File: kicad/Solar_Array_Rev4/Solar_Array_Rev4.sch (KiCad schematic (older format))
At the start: 23 parts

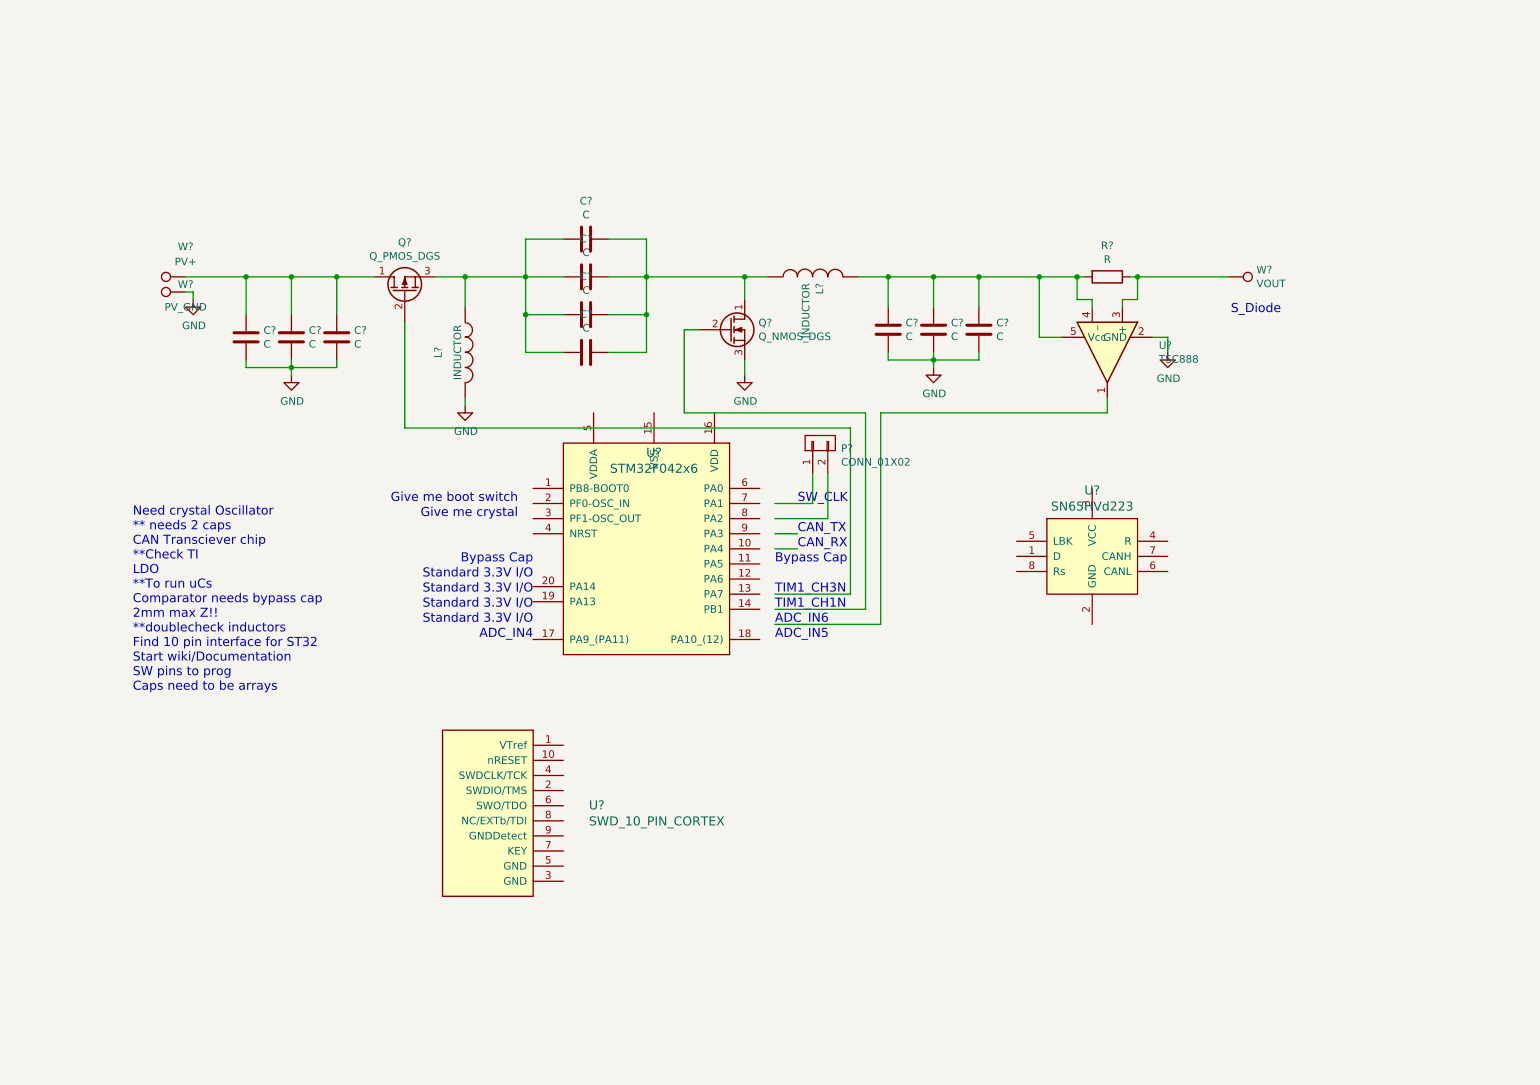
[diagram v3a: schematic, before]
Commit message: Rev1 GERBS.  Rev 4 Schematic editing/placement. -Regenerated rev1 gerbs -Added/updated schematic symbols for LDO, Crystal, CAN, uC -Added decoupling caps to various inputs -Reworked schematics because beauty
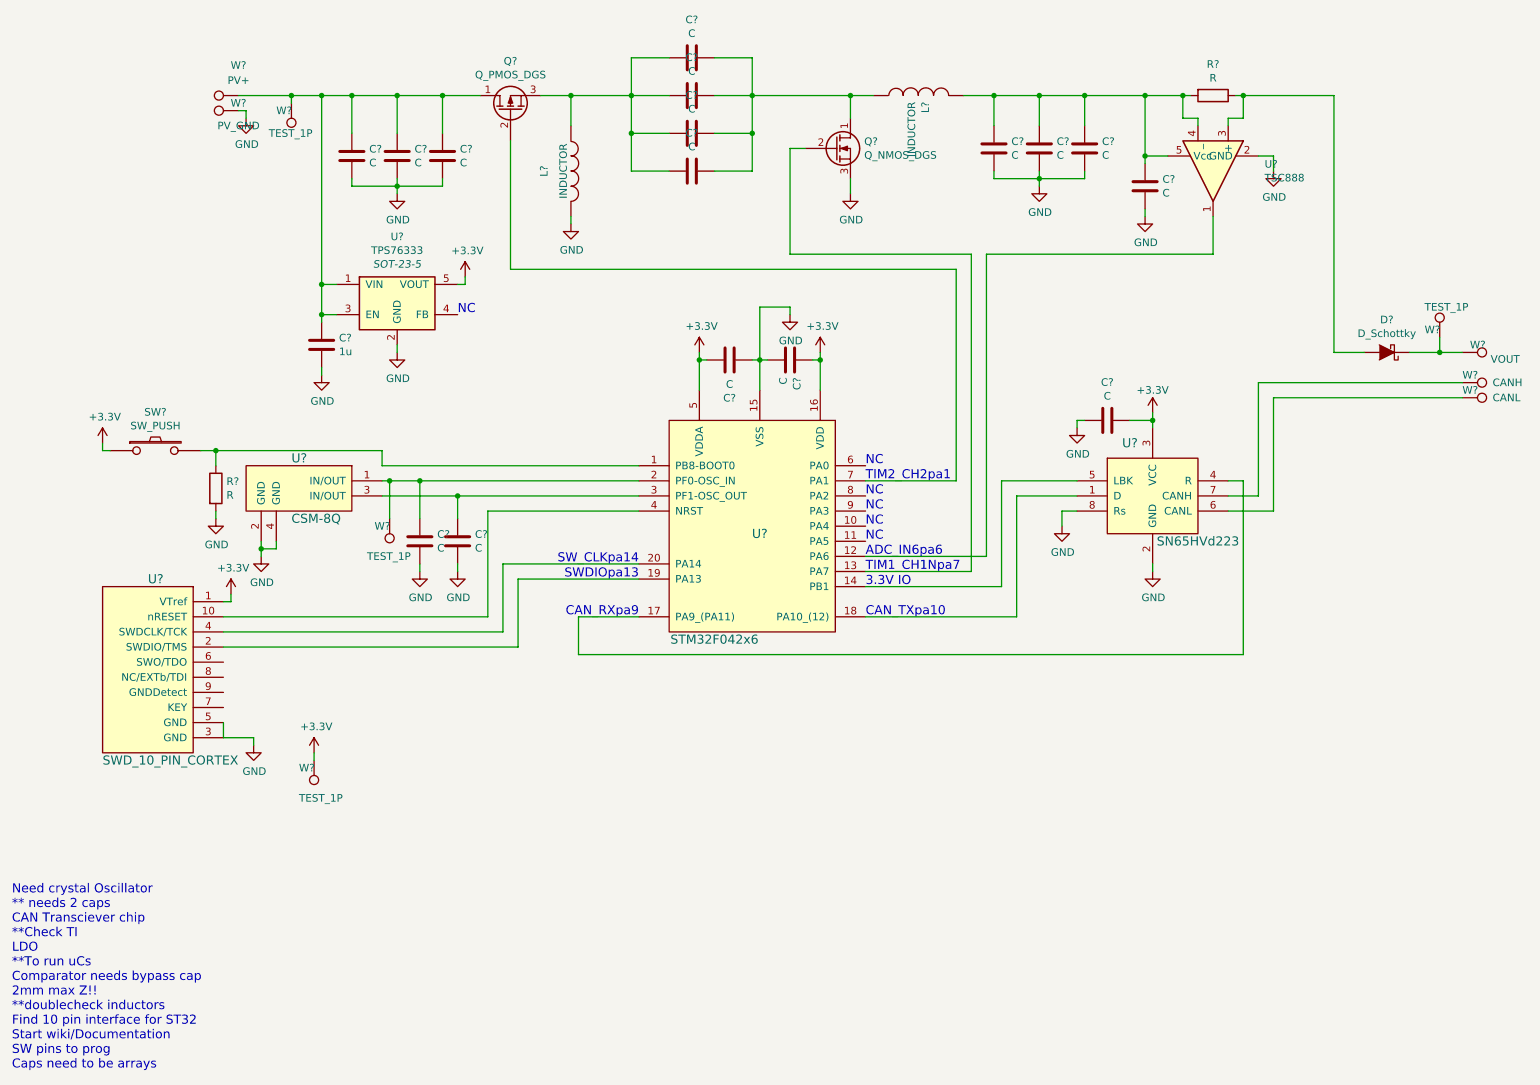
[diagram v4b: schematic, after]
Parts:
- removed P?: CONN_01X02, symbol CONN_01X02
- added C? (x6): C, symbol C
- added C?: 1u, symbol C
- added D?: D_Schottky, symbol D_Schottky
- added R?: R, symbol R
- added SW?: SW_PUSH, symbol SW_PUSH
- added U?: CSM-8Q, symbol CSM-8Q
- added U?: TPS76333, SOT-23-5, symbol TPS76333
- added W? (x4): TEST_1P, symbol TEST_1P
- added W?: CANH, symbol TEST_1P
- added W?: CANL, symbol TEST_1P
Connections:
- net labels added: +3.3V
- wire segments 62 -> 133
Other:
- note added: "3.3V IO"
- note added: "ADC_IN6pa6"
- note added: "CAN_RXpa9"
- note added: "CAN_TXpa10"
- note added: "NC"
- note added: "SWDIOpa13"
- note added: "SW_CLKpa14"
- note added: "TIM1_CH1Npa7"
- note added: "TIM2_CH2pa1"
- note removed: "ADC_IN4"
- note removed: "ADC_IN5"
- note removed: "ADC_IN6"
- note removed: "Bypass Cap"
- note removed: "CAN_RX"
- note removed: "CAN_TX"
- note removed: "Give me boot switch"
- note removed: "Give me crystal\n"
- note removed: "SW_CLK"
- note removed: "S_Diode"
- note removed: "Standard 3.3V I/O"
- note removed: "TIM1_CH1N"
- note removed: "TIM1_CH3N"
- moved on the sheet: C?, L?, Q?, R?, U?, W?
